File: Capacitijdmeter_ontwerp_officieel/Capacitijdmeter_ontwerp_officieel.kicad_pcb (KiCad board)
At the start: 2 copper layers, 15 parts, among them U0 74HC74, U1 74HC74, U12 7408, U14 74HC74, U15 74HC74, U18 7408, U2 7408, U20 74HC74, U21 74HC74, U4 74HC14, U5 74HC04, U8 74HC74, U9 74HC74

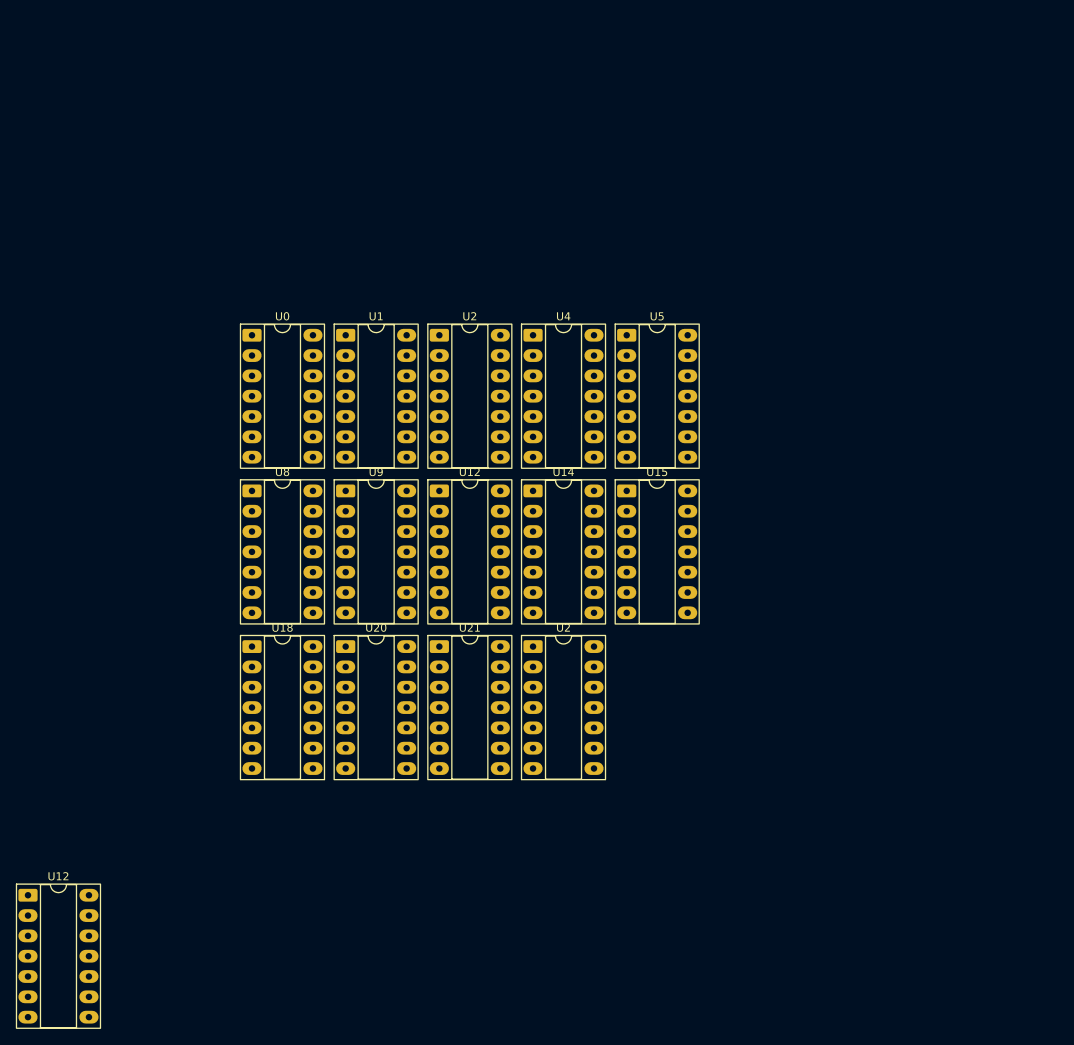
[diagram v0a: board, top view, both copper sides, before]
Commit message: add 4x3 switch
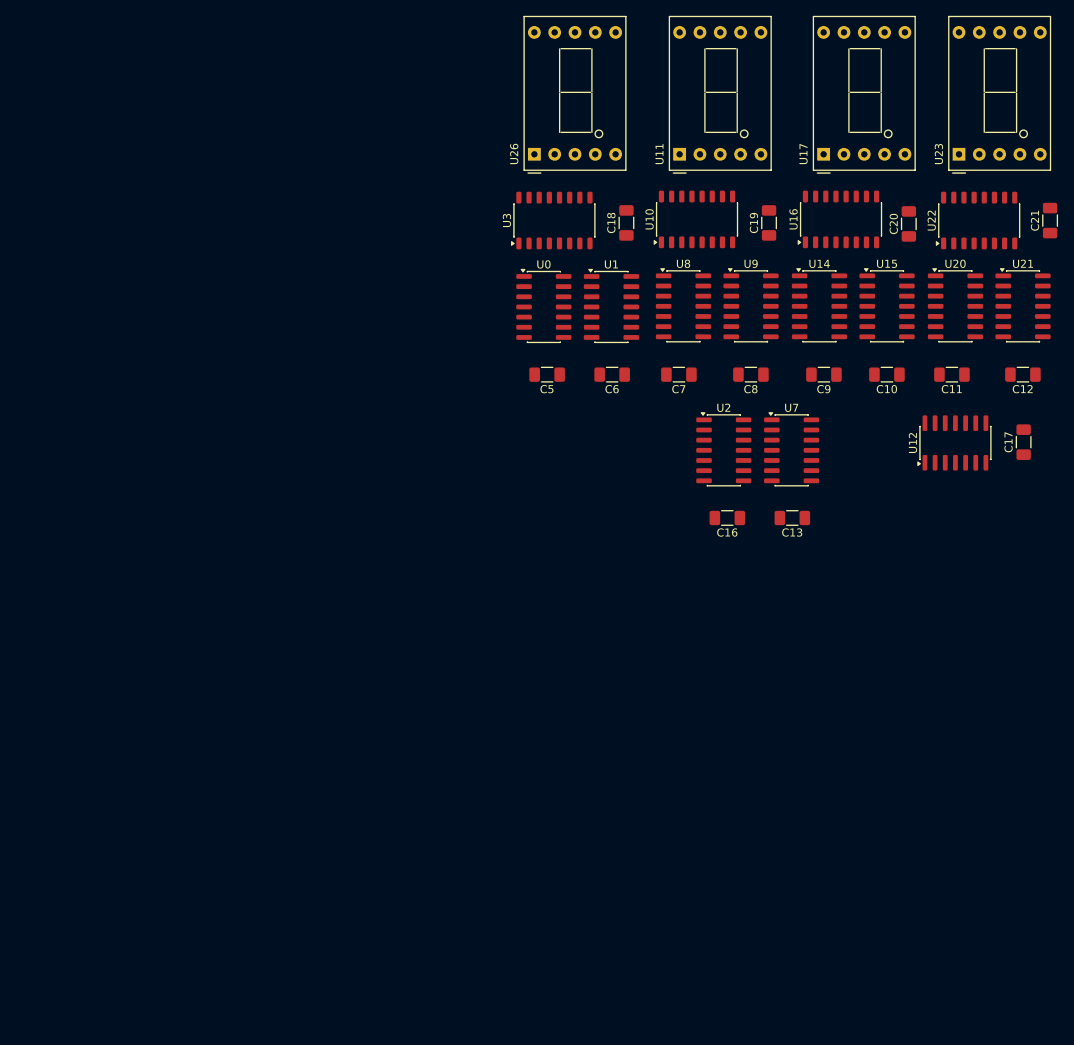
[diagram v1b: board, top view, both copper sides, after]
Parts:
- removed the U12 at (52.5, 151.6)
- removed the U12 at (104.0, 101.1)
- removed U18: 7408, Package_DIP:DIP-14_W7.62mm_Socket_LongPads
- removed the U2 at (115.7, 120.5)
- removed the U2 at (104.0, 81.6)
- removed U4: 74HC14, Package_DIP:DIP-14_W7.62mm_Socket_LongPads
- removed U5: 74HC04, Package_DIP:DIP-14_W7.62mm_Socket_LongPads
- added C10: 100nF, Capacitor_SMD:C_1206_3216Metric_Pad1.33x1.80mm_HandSolder, F.Cu at (159.9, 86.5)
- added C11: 100nF, Capacitor_SMD:C_1206_3216Metric_Pad1.33x1.80mm_HandSolder, F.Cu at (168.0, 86.5)
- added C12: 100nF, Capacitor_SMD:C_1206_3216Metric_Pad1.33x1.80mm_HandSolder, F.Cu at (176.9, 86.5)
- added C13: 100nF, Capacitor_SMD:C_1206_3216Metric_Pad1.33x1.80mm_HandSolder, F.Cu at (148.1, 104.5)
- added C16: 100nF, Capacitor_SMD:C_1206_3216Metric_Pad1.33x1.80mm_HandSolder, F.Cu at (140.0, 104.5)
- added C17: 100nF, Capacitor_SMD:C_1206_3216Metric_Pad1.33x1.80mm_HandSolder, F.Cu at (177.0, 95.0)
- added C18: 100nF, Capacitor_SMD:C_1206_3216Metric_Pad1.33x1.80mm_HandSolder, F.Cu at (127.3, 67.6)
- added C19: 100nF, Capacitor_SMD:C_1206_3216Metric_Pad1.33x1.80mm_HandSolder, F.Cu at (145.2, 67.6)
- added C20: 100nF, Capacitor_SMD:C_1206_3216Metric_Pad1.33x1.80mm_HandSolder, F.Cu at (162.7, 67.7)
- added C21: 100nF, Capacitor_SMD:C_1206_3216Metric_Pad1.33x1.80mm_HandSolder, F.Cu at (180.3, 67.3)
- added C5: 100nF, Capacitor_SMD:C_1206_3216Metric_Pad1.33x1.80mm_HandSolder, F.Cu at (117.4, 86.5)
- added C6: 100nF, Capacitor_SMD:C_1206_3216Metric_Pad1.33x1.80mm_HandSolder, F.Cu at (125.6, 86.5)
- added C7: 100nF, Capacitor_SMD:C_1206_3216Metric_Pad1.33x1.80mm_HandSolder, F.Cu at (133.9, 86.5)
- added C8: 100nF, Capacitor_SMD:C_1206_3216Metric_Pad1.33x1.80mm_HandSolder, F.Cu at (142.9, 86.5)
- added C9: 100nF, Capacitor_SMD:C_1206_3216Metric_Pad1.33x1.80mm_HandSolder, F.Cu at (152.0, 86.5)
- added U10: 4511, Package_SO:JEITA_SOIC-16_3.9x9.9mm_P1.27mm, F.Cu at (136.2, 67.1)
- added U11: ~, Display_7Segment:D1X8K, F.Cu at (134.0, 59.0)
- added U12: 7408, Package_SO:SOIC-14_3.9x8.7mm_P1.27mm, F.Cu at (168.5, 95.1)
- added U16: 4511, Package_SO:JEITA_SOIC-16_3.9x9.9mm_P1.27mm, F.Cu at (154.2, 67.1)
- added U17: ~, Display_7Segment:D1X8K, F.Cu at (152.0, 59.0)
- added U2: 7408, Package_SO:SOIC-14_3.9x8.7mm_P1.27mm, F.Cu at (139.5, 96.0)
- added U22: 4511, Package_SO:JEITA_SOIC-16_3.9x9.9mm_P1.27mm, F.Cu at (171.4, 67.3)
- added U23: ~, Display_7Segment:D1X8K, F.Cu at (168.9, 59.0)
- added U26: ~, Display_7Segment:D1X8K, F.Cu at (115.8, 59.0)
- added U3: 4511, Package_SO:JEITA_SOIC-16_3.9x9.9mm_P1.27mm, F.Cu at (118.3, 67.3)
- added U7: 74HC02, Package_SO:SOIC-14_3.9x8.7mm_P1.27mm, F.Cu at (148.0, 96.0)
- U0, U1, U14, U15, U20, U21, U8, U9: footprint Package_DIP:DIP-14_W7.62mm_Socket_LongPads -> Package_SO:SOIC-14_3.9x8.7mm_P1.27mm
- moved U20 87.3 mm to (168.5, 78.0)
- moved U21 84.5 mm to (176.9, 78.0)
- moved U8 58.7 mm to (134.5, 78.0)
- moved U9 55.7 mm to (142.9, 78.0)
- moved U14 42.6 mm to (151.5, 78.0)
- moved U15 39.9 mm to (159.9, 78.0)
- moved U0 36.7 mm to (117.0, 78.1)
- moved U1 33.4 mm to (125.5, 78.1)
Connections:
- U0 pad 11: Net-(U0A-~{Q}) -> Net-(U0A-D)
- U0 pad 3: Net-(U0A-C) -> V_{clk0}
- U0 pad 5: Net-(U0A-D) -> Net-(U0A-Q)
- U0 pad 6: Net-(U0A-~{Q}) -> Net-(U0A-D)
- U14 pad 11: Net-(U14A-~{Q}) -> Net-(U14A-D)
- U14 pad 3: Net-(U14A-C) -> V_{clk2}
- U14 pad 5: Net-(U14A-D) -> Net-(U14A-Q)
- U14 pad 6: Net-(U14A-~{Q}) -> Net-(U14A-D)
- U20 pad 11: Net-(U20A-~{Q}) -> Net-(U20A-D)
- U20 pad 5: Net-(U20A-D) -> Net-(U20A-Q)
- U20 pad 6: Net-(U20A-~{Q}) -> Net-(U20A-D)
- U8 pad 11: Net-(U8A-~{Q}) -> Net-(U8A-D)
- U8 pad 2: Net-(U10-DA) -> Net-(U8A-D)
- U8 pad 3: Net-(U8A-C) -> V_{clk1}
- U8 pad 6: Net-(U8A-~{Q}) -> Net-(U8A-D)

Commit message: add traces
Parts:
- turned C18 to -90 degrees
- turned C5 to 0 degrees
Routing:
- net +5V: track 0.00 -> 58.3 mm
- net V_{clk0}: track 0.00 -> 43.2 mm, vias 0 -> 2
- net Net-(U0B-Q): track 0.00 -> 38.5 mm, vias 0 -> 2
- net V_{a3}: track 0.00 -> 30.4 mm, vias 0 -> 1
- net V_{b3}: track 0.00 -> 29.6 mm, vias 0 -> 1
- net V_{g3}: track 0.00 -> 25.0 mm, vias 0 -> 1
- net V_{f3}: track 0.00 -> 23.8 mm, vias 0 -> 1
- net Net-(U1B-Q): track 0.00 -> 19.0 mm
- net Net-(U1A-Q): track 0.00 -> 18.7 mm
- net Net-(U0A-~{R}): track 0.00 -> 17.2 mm, vias 0 -> 2
- net GND: track 0.00 -> 16.5 mm
- net Net-(U0A-D): track 0.00 -> 13.7 mm
- net Net-(U0A-Q): track 0.00 -> 12.7 mm, vias 0 -> 2
- net Net-(U1A-D): track 0.00 -> 11.4 mm, vias 0 -> 3
- net V_{c3}: track 0.00 -> 11.2 mm, vias 0 -> 1
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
